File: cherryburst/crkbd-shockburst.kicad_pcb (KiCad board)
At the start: 4 copper layers, 272 x 112 mm, 233 parts, among them J201 USB_C_Receptacle_USB2.0, J202 tag-connect-swd, J203 LCD, J5 Breakaway_Tabs, J501 tag-connect-swd, J502 USB_C_Receptacle_USB2.0, J503 LCD, J601 tag-connect-swd, J602 USB_A, SW101 SW_SPDT, SW102 SW_SPDT, SW301 SW_Push, SW302 SW_Push, SW303 SW_Push, SW304 SW_Push, SW305 SW_Push, SW306 SW_Push, SW307 SW_Push, SW308 SW_Push, SW309 SW_Push, SW310 SW_Push, SW311 SW_Push, SW312 SW_Push, SW313 SW_Push, SW314 SW_Push, SW315 SW_Push, SW316 SW_Push, SW317 SW_Push, SW318 SW_Push, SW319 SW_Push, SW320 SW_Push, SW321 SW_Push, SW401 SW_Push, SW402 SW_Push, SW403 SW_Push, SW404 SW_Push, SW405 SW_Push, SW406 SW_Push, SW407 SW_Push, SW408 SW_Push, SW409 SW_Push, SW410 SW_Push, SW411 SW_Push, SW412 SW_Push, SW413 SW_Push, SW414 SW_Push, SW415 SW_Push, SW416 SW_Push, SW417 SW_Push, SW418 SW_Push, SW419 SW_Push, SW420 SW_Push, SW421 SW_Push, SW601 SW_Push, U201 nRF52833-QDxx, U202 USBLC6-2SC6, U203 TPS70630DBVR, U204 MCP73832-2-OT, U501 nRF52833-QDxx, U502 USBLC6-2SC6, U503 MCP73832-2-OT, U504 TPS70630DBVR, U601 nRF52833-QDxx, U602 USBLC6-2SC6, Y201 32 MHz, Y501 32 MHz, Y601 32 MHz

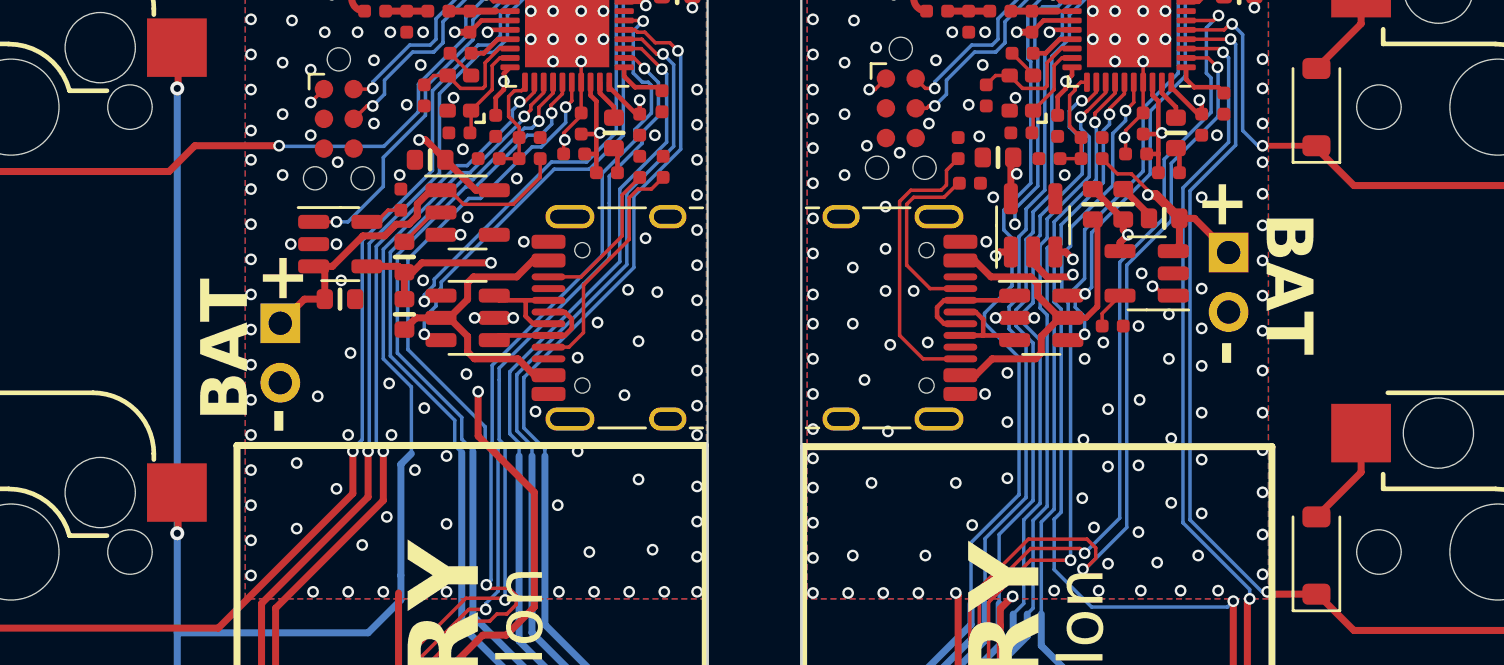
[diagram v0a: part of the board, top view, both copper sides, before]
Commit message: Some small fixes for battery connector
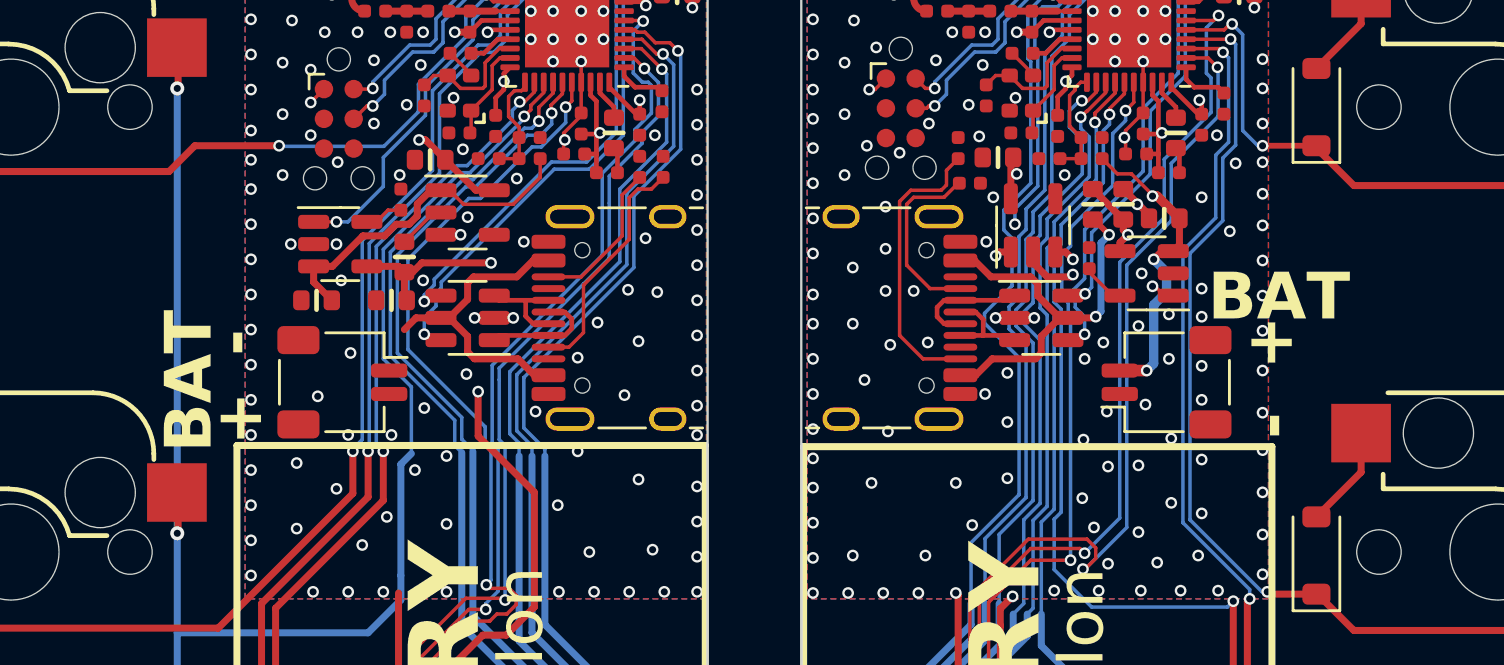
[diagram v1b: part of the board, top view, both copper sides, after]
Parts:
- removed BT201, BT501: Battery_Cell, connectors:1x2_2.54mm
- added J204: Conn_01x02_MountingPin, Connector_JST:JST_SH_SM02B-SRSS-TB_1x02-1MP_P1.00mm_Horizontal, F.Cu at (131.4, 74.5)
- added J504: Conn_01x02_MountingPin, Connector_JST:JST_SH_SM02B-SRSS-TB_1x02-1MP_P1.00mm_Horizontal, F.Cu at (166.6, 74.5)
- moved R506 3.07 mm to (163.3, 69.2), turned to -90 degrees
- moved C202 1.00 mm to (130.3, 71.0), turned to 180 degrees
- moved FB201 0.81 mm to (133.5, 71.0), turned to 180 degrees
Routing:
- net /Right Keyboard Controller/VBAT: track 17.0 -> 22.1 mm, vias 2 -> 4
- net /Left Keyboard Controller/VBAT: track 16.9 -> 14.6 mm
- net /Right Keyboard Controller/VIN_USB: track 16.8 -> 17.5 mm, vias 0 -> 2
- net GND: vias 422 -> 424
